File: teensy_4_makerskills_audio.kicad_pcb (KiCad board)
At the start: 2 copper layers, 17.8 x 35.6 mm, 12 parts, among them J1 Teensy, J2 Teensy, J3 Output, J4 minijack, U1 PT8211, U2 INMP441

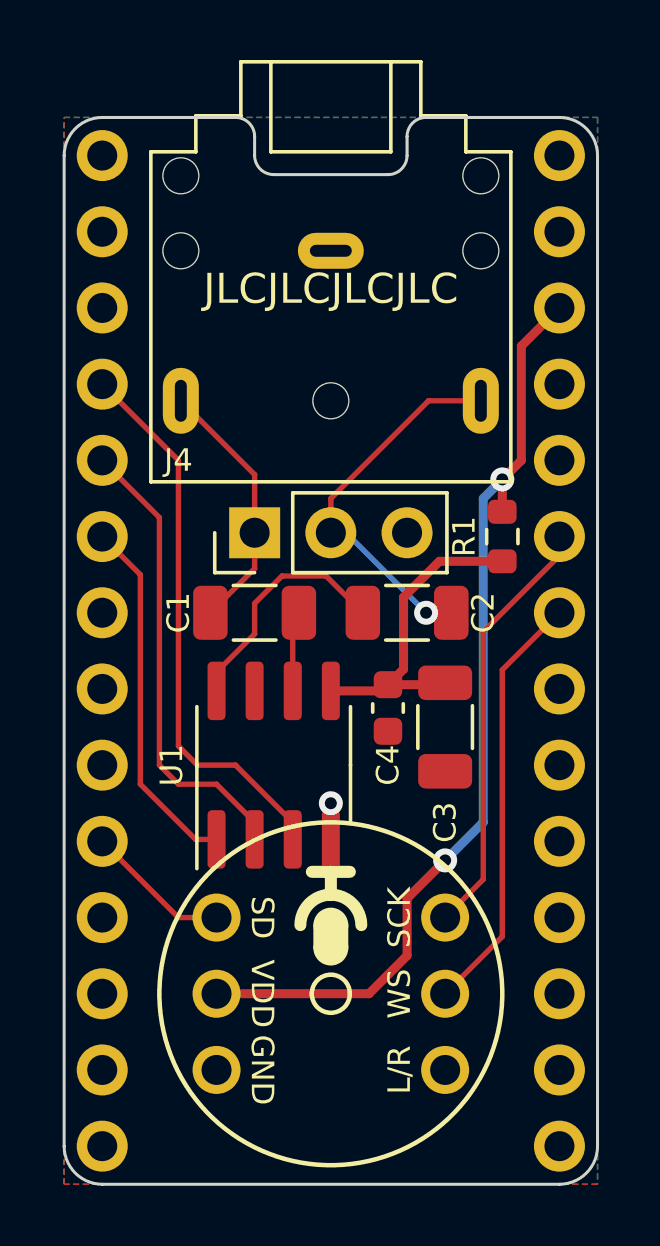
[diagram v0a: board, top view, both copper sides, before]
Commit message: Pin usage marked, PCBA teensy pins, mic smd sockets
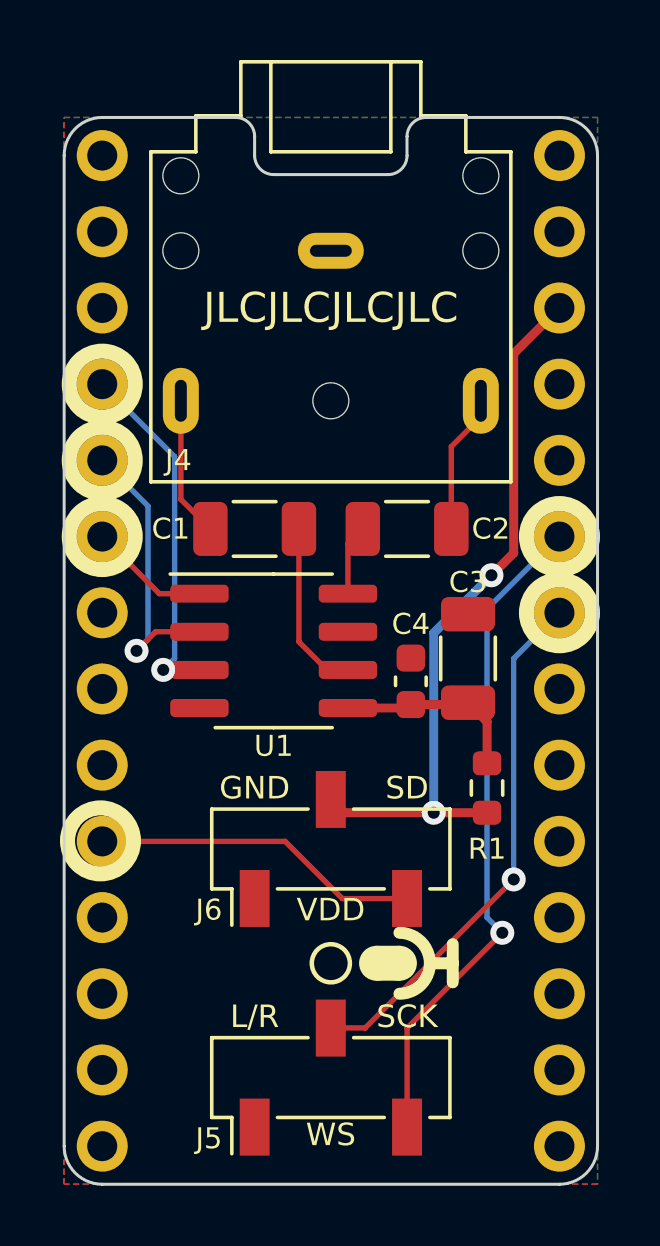
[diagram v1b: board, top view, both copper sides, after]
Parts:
- removed J3: Output, Connector_PinHeader_2.54mm:PinHeader_1x03_P2.54mm_Vertical
- removed U2: INMP441, teensy:INMP441
- added J5: Conn_01x03, Connector_PinSocket_2.54mm:PinSocket_1x03_P2.54mm_Vertical_SMD_Pin1Left, F.Cu at (69.8, 81.5)
- added J6: Conn_01x03, Connector_PinSocket_2.54mm:PinSocket_1x03_P2.54mm_Vertical_SMD_Pin1Left, F.Cu at (69.8, 73.9)
- moved R1 8.40 mm to (75.1, 71.9), turned to 90 degrees
- moved U1 3.81 mm to (67.9, 67.3), turned to 0 degrees
- moved C1 2.79 mm to (67.3, 63.2)
- moved C2 2.79 mm to (72.4, 63.2)
- moved C3 2.41 mm to (74.4, 67.6), turned to 90 degrees
- moved C4 1.17 mm to (72.5, 68.3), turned to 90 degrees
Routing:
- net RIGHT: track 12.8 -> 4.68 mm, vias 1 -> 0
- net DAC_BCK: track 12.1 -> 4.03 mm
- net ADC_SCK: track 14.3 -> 22.2 mm, vias 0 -> 1
- net +3.3V: track 31.7 -> 24.0 mm
- net DAC_DIN: track 18.5 -> 11.9 mm, vias 0 -> 1
- net ADC_SD: track 4.86 -> 11.0 mm
- net DAC_WS: track 15.5 -> 9.50 mm, vias 0 -> 1
- net Net-(U1-R): track 7.93 -> 2.36 mm
- net +3.3VA: track 10.8 -> 6.36 mm
- net LEFT: track 8.69 -> 4.68 mm
- net ADC_WS: track 14.3 -> 17.7 mm, vias 0 -> 1
- net Net-(U1-L): track 2.69 -> 5.78 mm
- net GND: track 1.77 -> 0.00 mm, vias 1 -> 0
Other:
- board text added: "Music & Technology mic+dac cape for Teensy 4.x 08-07-2027 Ward Slager"
- board text added: "Teensy USB"
- board text removed: "Music & Technology mic+dac cape for Teensy 4.0"
- board text removed: "USB this side"
